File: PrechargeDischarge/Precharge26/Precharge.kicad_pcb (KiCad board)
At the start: 2 copper layers, 203 x 98 mm, 129 parts, among them J1 MicroFit, J2 Mini-Fit_Jr_5566-04A, J3 Micro-Fit 43045-0212, J4 Micro-Fit 43045-0212, K1 OMRON-G2RL-24, K2 G7L-2A-X-L, K4 Relay_SPST-NC, Q1 2N7002, Q2 MMBT3906, Q3 2N7002, Q5 NMOS, U1 TJA1051T-3, U10 LM393, U11 4N35, U2 SPAN02A-12, U3 Teensy4.0, U4 LM1117-5.0, U5 4N35, U6 4N35, U7 LM331, U8 LM331, U9 LM2904

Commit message: precharge/discharge. charging
removed discharge ffrom precharge and put it on board out of battery, updqted charging according to discharge
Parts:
- removed ? (x2): , 
- removed D13: D, Diode_SMD:D_SMA
- removed J4: Micro-Fit 43045-0212, Connector_Molex:Molex_Micro-Fit_3.0_43045-0212_2x01_P3.00mm_Vertical
- removed K4: Relay_SPST-NC, Precharge:Discharge_relay
- removed Q5: NMOS, Package_TO_SOT_SMD:SOT-23
- removed R50: HSA503K0J, Precharge:Discharge_Resistor
- removed R51: 10k, Resistor_SMD:R_1206_3216Metric
- added H1: MountingHole, MountingHole:MountingHole_3.2mm_M3, F.Cu at (3.48, 3.48)
- D10, D11, D6: footprint Diode_SMD:D_SOT-23_ANK -> Package_TO_SOT_SMD:SOT-23
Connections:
- D2 pad 2: unconnected-(D2-A-Pad2) -> Net-(D2-Pad2)
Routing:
- net GNDS: track 367.4 -> 261.7 mm
- net Net-(D11-K): track 0.00 -> 64.3 mm, vias 0 -> 1
- net Net-(D10-K): track 0.00 -> 47.5 mm
- net +12V: track 227.7 -> 184.8 mm, vias 2 -> 0
- net GLV-: track 364.8 -> 334.3 mm
- net /IR+_MC: track 29.7 -> 0.00 mm
- net Net-(K4-Pad4): track 18.3 -> 0.00 mm
- net /MSD_IN: track 15.7 -> 0.00 mm
- net Net-(D13-A): track 14.1 -> 0.00 mm
- net GLV+: track 100.5 -> 106.8 mm
- net /VinTS: track 48.3 -> 46.6 mm
- net /TS-: vias 9 -> 11
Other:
- board size 203 x 98 mm -> 133 x 98 mm
- board text removed: "5.3mm"
- board text removed: "Precharge Module v1.1"

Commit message: Molex Microfit
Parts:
- removed H1: MountingHole, MountingHole:MountingHole_3.2mm_M3
- J2: footprint Mini-Fit-Jr-4.20mm-pitch:Molex-Mini-Fit-Jr-4-pin-P4.2mm-RowP4.2mm -> Precharge:MICROFIT-4PIN
- J3: value Micro-Fit 43045-0212 -> 447690401; footprint Connector_Molex:Molex_Micro-Fit_3.0_43045-0212_2x01_P3.00mm_Vertical -> Precharge:MICROFIT-4PIN
- moved J2 3.77 mm to (91.2, 59.5), turned to 90 degrees
- moved J3 3.64 mm to (75.7, 133.9), turned to 90 degrees
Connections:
- D2 pad 2: Net-(D2-Pad2) -> unconnected-(D2-A-Pad2)
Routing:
- net Net-(J2-Pin_1): track 47.1 -> 43.4 mm
- net /VinTS: track 46.6 -> 49.2 mm
- net /TS-: track 8.10 -> 7.33 mm

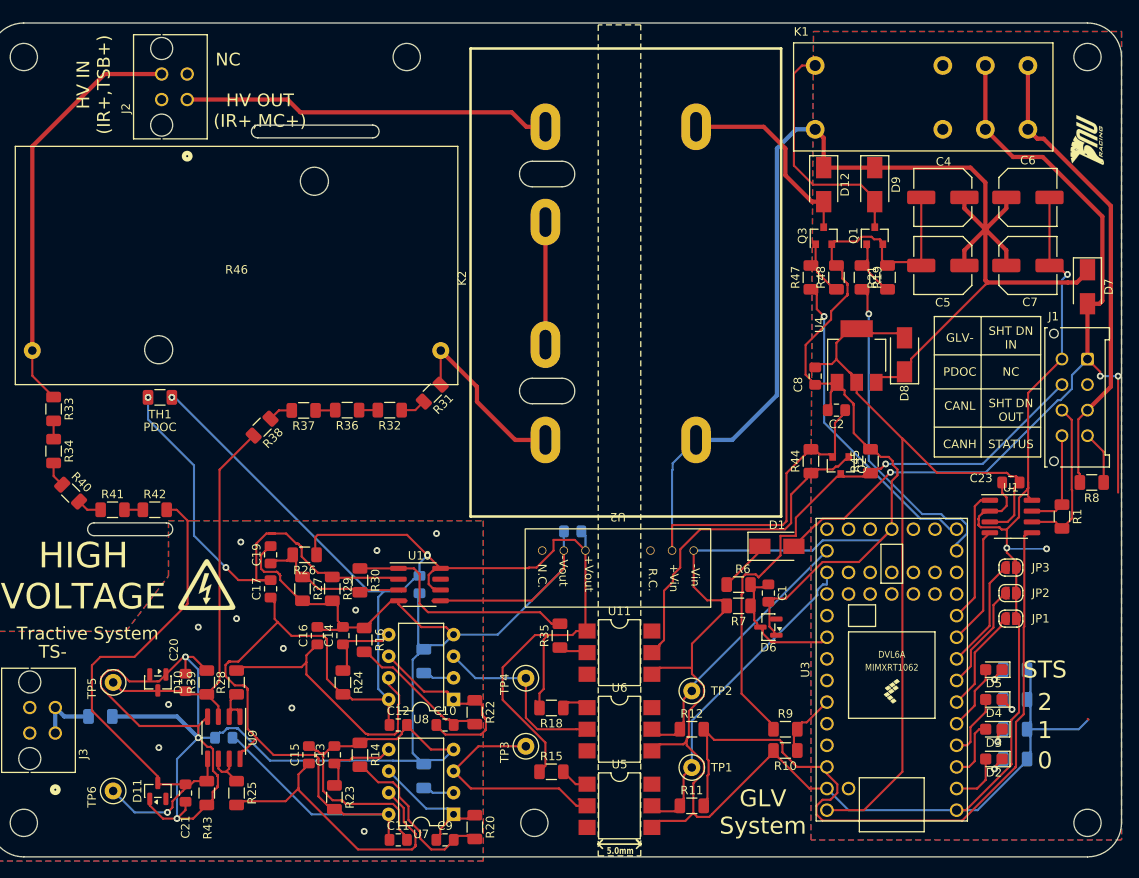
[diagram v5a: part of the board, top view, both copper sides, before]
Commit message: Precharge Testing
Uploaded precharge testing data, settled on 1.5k ohm resistor to precharge MC around 1s
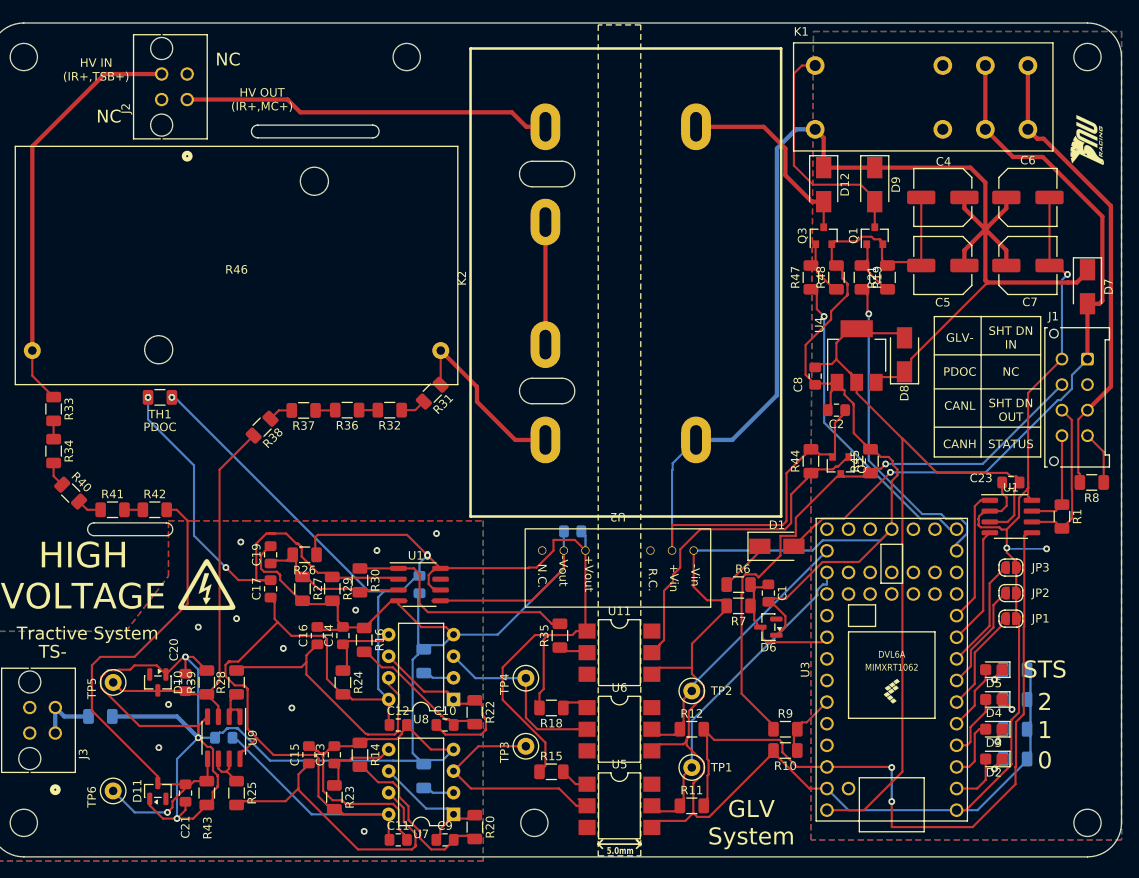
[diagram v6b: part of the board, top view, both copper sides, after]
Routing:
- net GLV+: track 106.8 -> 88.4 mm, vias 3 -> 1
- net GLV-: track 334.3 -> 328.1 mm
- net +3V3: track 88.8 -> 88.2 mm, vias 0 -> 2

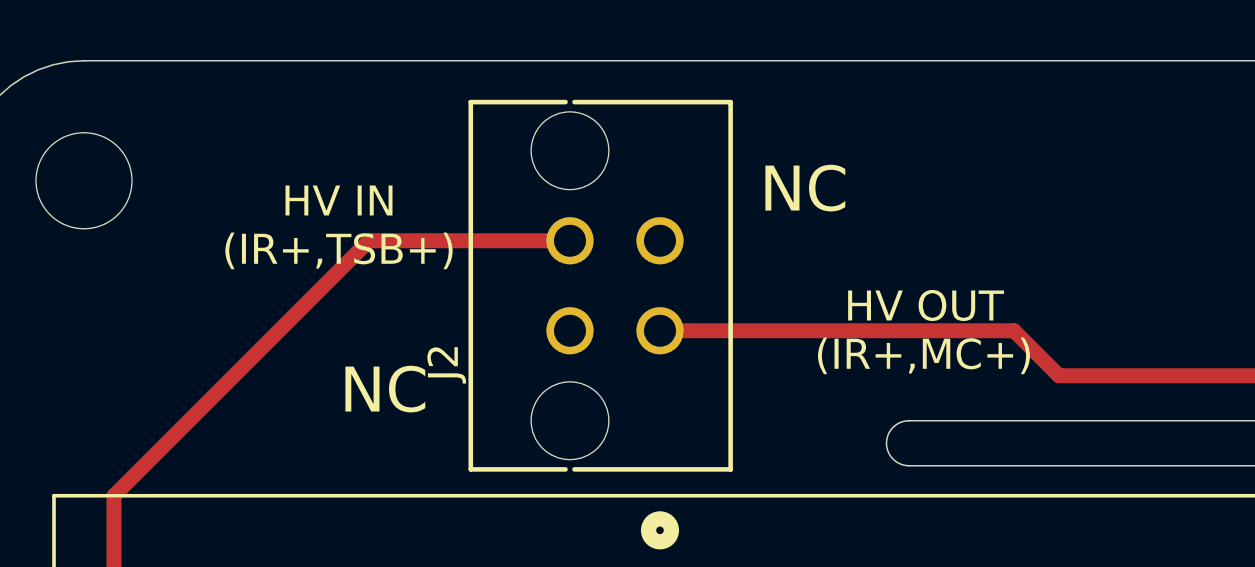
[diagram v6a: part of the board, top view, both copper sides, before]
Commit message: started TS schematic
TS schematic for ESF
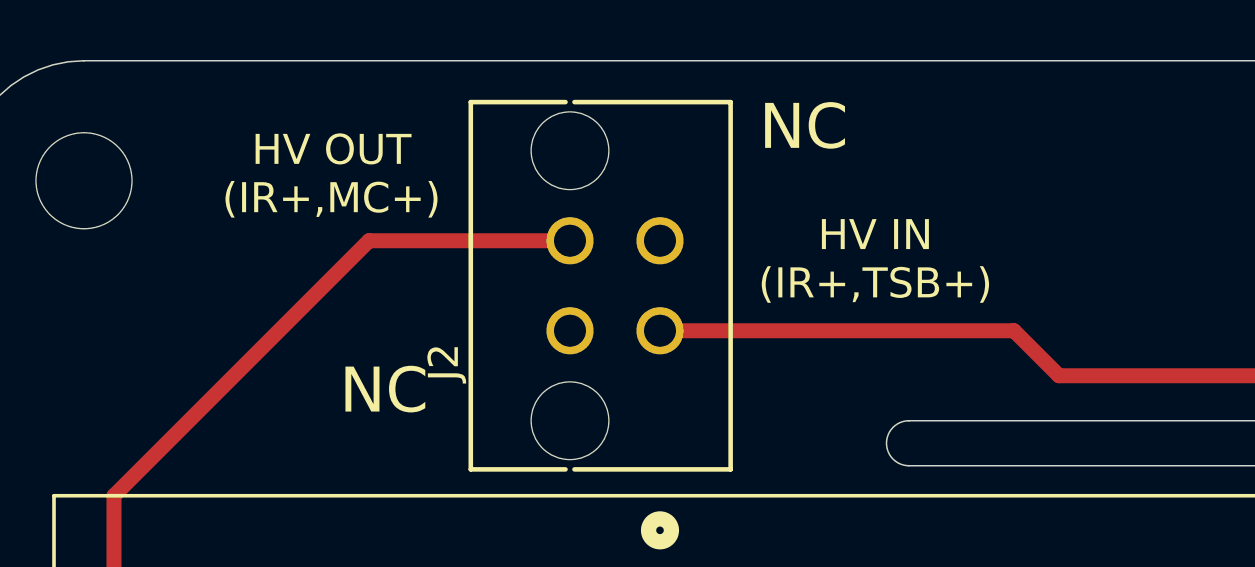
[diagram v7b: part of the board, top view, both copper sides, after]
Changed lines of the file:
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@@
 	)
 	(gr_text "HV OUT \n(IR+,MC+)"
-		(at 100 59.5 0)
+		(at 80.25 54.28 0)
 		(layer "F.SilkS")
 		(effects
@@
 	)
 	(gr_text "NC"
-		(at 96 54.8 0)
+		(at 95.99 52.71 0)
 		(layer "F.SilkS")
 		(effects
@@
 	)
 	(gr_text "HV IN\n(IR+,TSB+)"
-		(at 80.5 56 0)
-		(layer "F.SilkS")
-		(effects
+		(at 98.38 57.12 0)
+		(layer "F.SilkS")
+		(effects

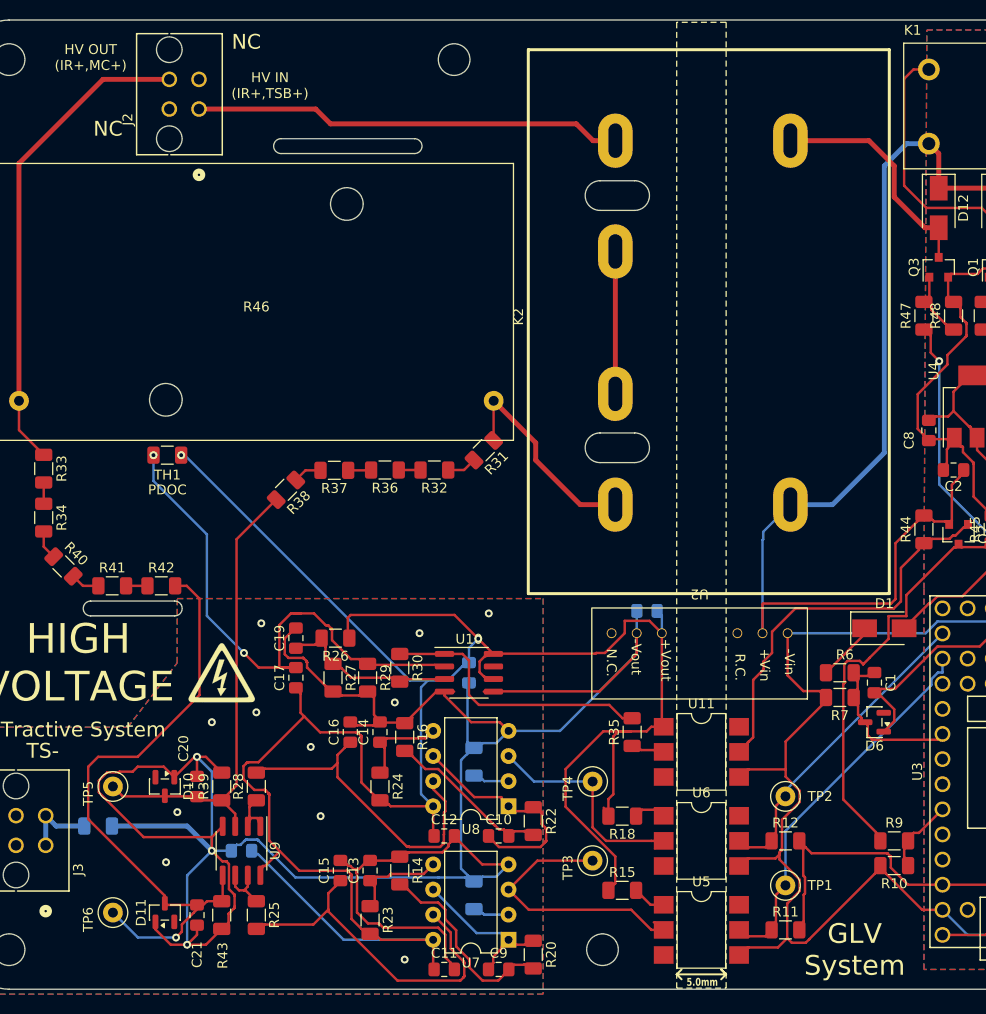
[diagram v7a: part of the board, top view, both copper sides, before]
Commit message: prechaarge
fixed precharge footprin
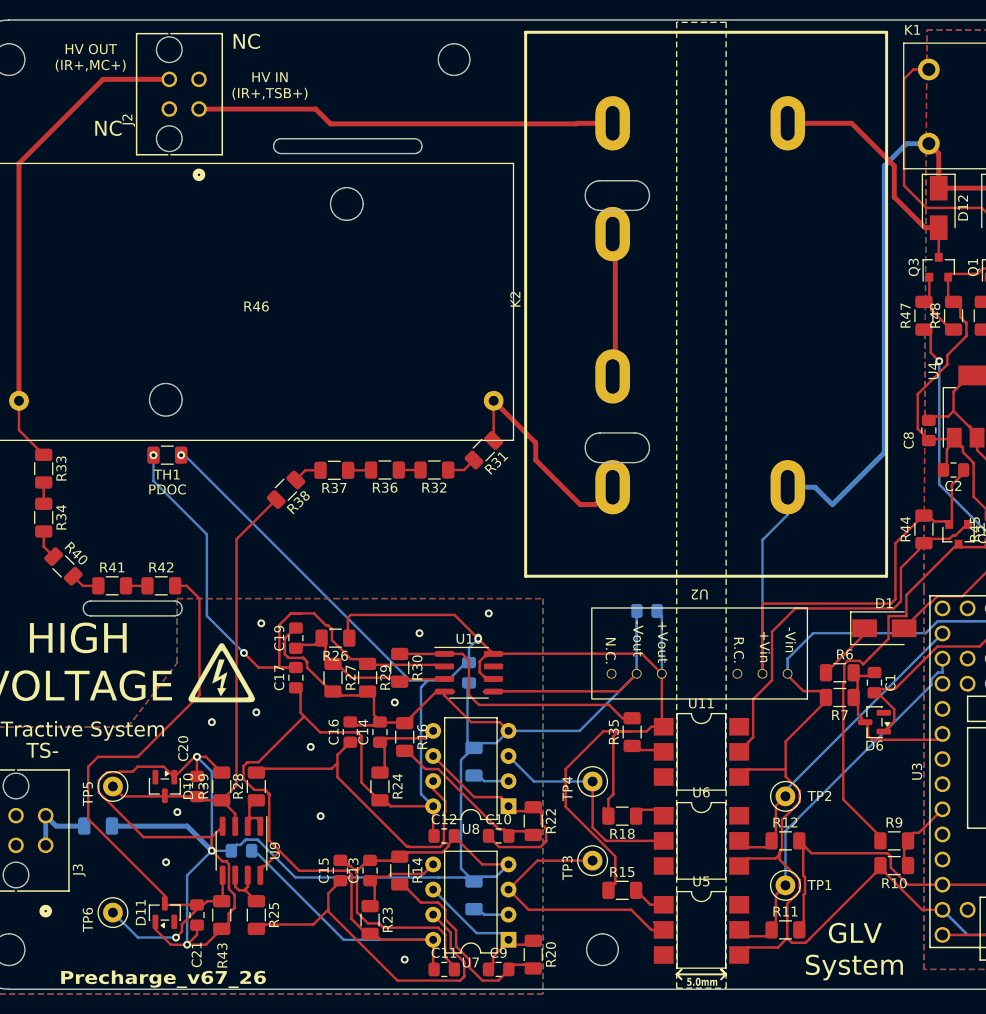
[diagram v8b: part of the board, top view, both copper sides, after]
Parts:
- moved K2 1.78 mm to (150.7, 97.7)
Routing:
- net +12V: track 184.8 -> 194.7 mm
- net GNDS: track 261.5 -> 259.7 mm
- net GLV-: track 328.1 -> 326.4 mm
- net +12P: track 242.4 -> 241.3 mm
- net Net-(D12-A): track 23.5 -> 24.5 mm
- net Net-(J2-Pin_1): track 43.4 -> 42.5 mm
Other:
- board text added: "Precharge_v67_26"
